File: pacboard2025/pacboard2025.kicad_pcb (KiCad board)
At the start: 4 copper layers, 80 x 80 mm, 28 parts, among them J1 XT30 Male Connector, U2 D24V50F5, U3 ProS3, U6 BNO085

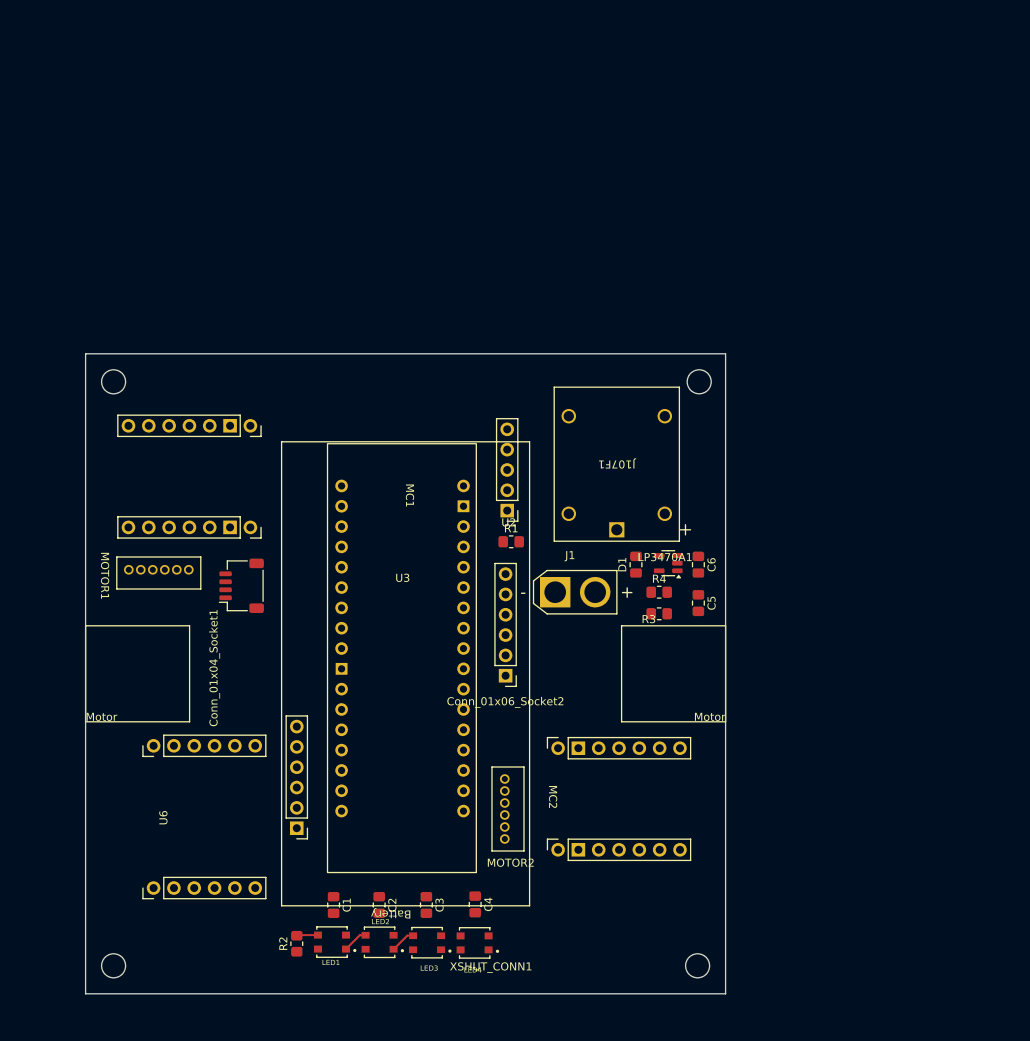
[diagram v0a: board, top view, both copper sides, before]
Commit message: changed layout
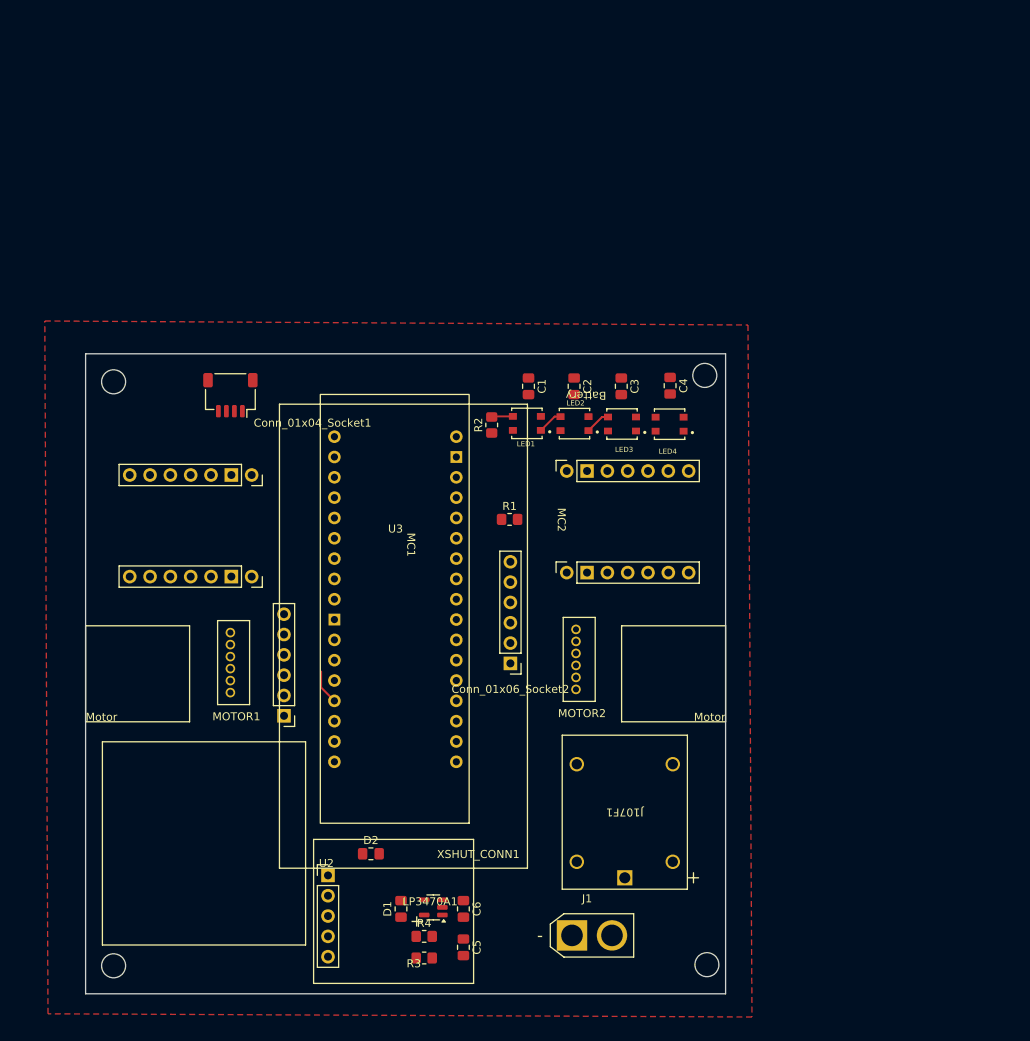
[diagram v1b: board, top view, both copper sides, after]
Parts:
- removed U6: BNO085, board1_footprints:BNU0085
- added D2: D, Capacitor_SMD:C_0805_2012Metric_Pad1.18x1.45mm_HandSolder, F.Cu at (115.7, 162.5)
- moved C1 69.3 mm to (135.4, 104.1)
- moved C2 69.3 mm to (141.1, 104.1)
- moved C3 69.3 mm to (147.0, 104.1)
- moved LED2 69.3 mm to (141.1, 108.7)
- moved LED3 69.3 mm to (147.1, 108.8)
- moved R2 69.3 mm to (130.8, 108.9)
- moved C4 69.3 mm to (153.1, 104.0)
- moved LED1 69.3 mm to (135.2, 108.7)
- moved LED4 69.3 mm to (153.0, 108.8)
- moved C5 52.1 mm to (127.2, 174.2)
- moved C6 52.1 mm to (127.2, 169.4)
- moved D1 52.1 mm to (119.4, 169.4)
- moved LP3470A1 52.1 mm to (123.5, 169.2)
- moved R3 52.1 mm to (122.3, 175.5)
- moved R4 52.1 mm to (122.3, 172.8)
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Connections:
- U2 pad 1: /5V -> Net-(D2-A)
- U3 pad 23: /UART_RX -> unconnected-(U3-RX-Pad23)
- U3 pad 24: /UART_TX -> unconnected-(U3-TX-Pad24)
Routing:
- net /XSHUT_TOF2: track 0.00 -> 4.34 mm
- added copper zone on In1.Cu, net /5V
- added copper zone on F.Cu, net /GND
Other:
- outline, holes or cut-outs redrawn

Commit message: Layout
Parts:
- moved MOTOR2 16.9 mm to (133.2, 149.3)
- moved XSHUT_CONN1 16.5 mm to (107.1, 128.9)
- moved MOTOR1 12.7 mm to (88.8, 126.1), turned to 90 degrees
- moved Conn_01x06_Socket2 10.4 mm to (133.4, 128.3)
- moved R1 9.20 mm to (133.1, 111.5)
- moved MC1 8.90 mm to (106.7, 112.6)
- moved Conn_01x04_Socket1 8.36 mm to (103.0, 98.4)
- moved U3 6.95 mm to (119.7, 123.8)
- moved C1 2.93 mm to (135.8, 101.2)
- moved C2 2.93 mm to (141.5, 101.2)
- moved C3 2.93 mm to (147.4, 101.2)
- moved LED1 2.93 mm to (135.6, 105.8)
- moved LED3 2.93 mm to (147.5, 105.9)
- moved R2 2.93 mm to (131.2, 106.0)
- moved C4 2.93 mm to (153.5, 101.1)
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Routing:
- net /XSHUT_TOF6: track 0.00 -> 99.7 mm
- net /2_ENCB: track 0.00 -> 46.2 mm
- net /5V: track 43.0 -> 0.11 mm
- net /1_ENCA: track 0.00 -> 41.7 mm, vias 0 -> 1
- net unconnected-(MC1-CS-Pad8): track 0.00 -> 35.9 mm, vias 0 -> 1
- net /1_ENCB: track 0.00 -> 35.1 mm, vias 0 -> 1
- net /SERIAL_CLOCK_LINE: track 0.00 -> 33.9 mm, vias 0 -> 1
- net /XSHUT_TOF3: track 0.00 -> 25.3 mm, vias 0 -> 1
- net /GND: track 0.00 -> 25.0 mm
- net /1_PWM2: track 0.00 -> 21.6 mm, vias 0 -> 1
- net /MOTOR2_V+: track 0.00 -> 19.7 mm
- net /XSHUT_TOF5: track 0.00 -> 12.9 mm
- net /XSHUT_TOF4: track 0.00 -> 12.9 mm
- net unconnected-(U3-IO0-Pad11): track 0.00 -> 9.03 mm
- net /INTR_TOF6: track 0.00 -> 9.03 mm
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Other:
- board size 80 x 80 mm -> 80 x 85 mm

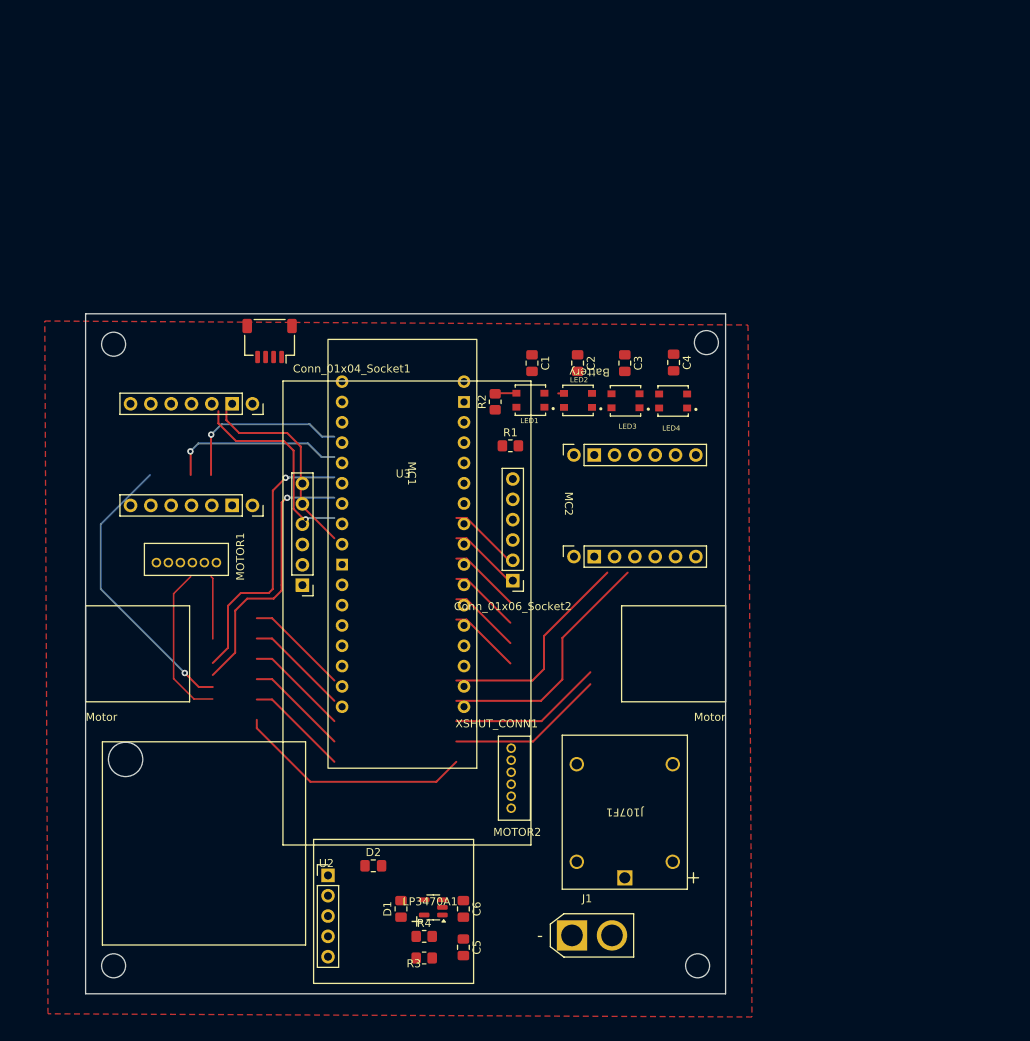
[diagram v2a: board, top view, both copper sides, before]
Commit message: layout updated
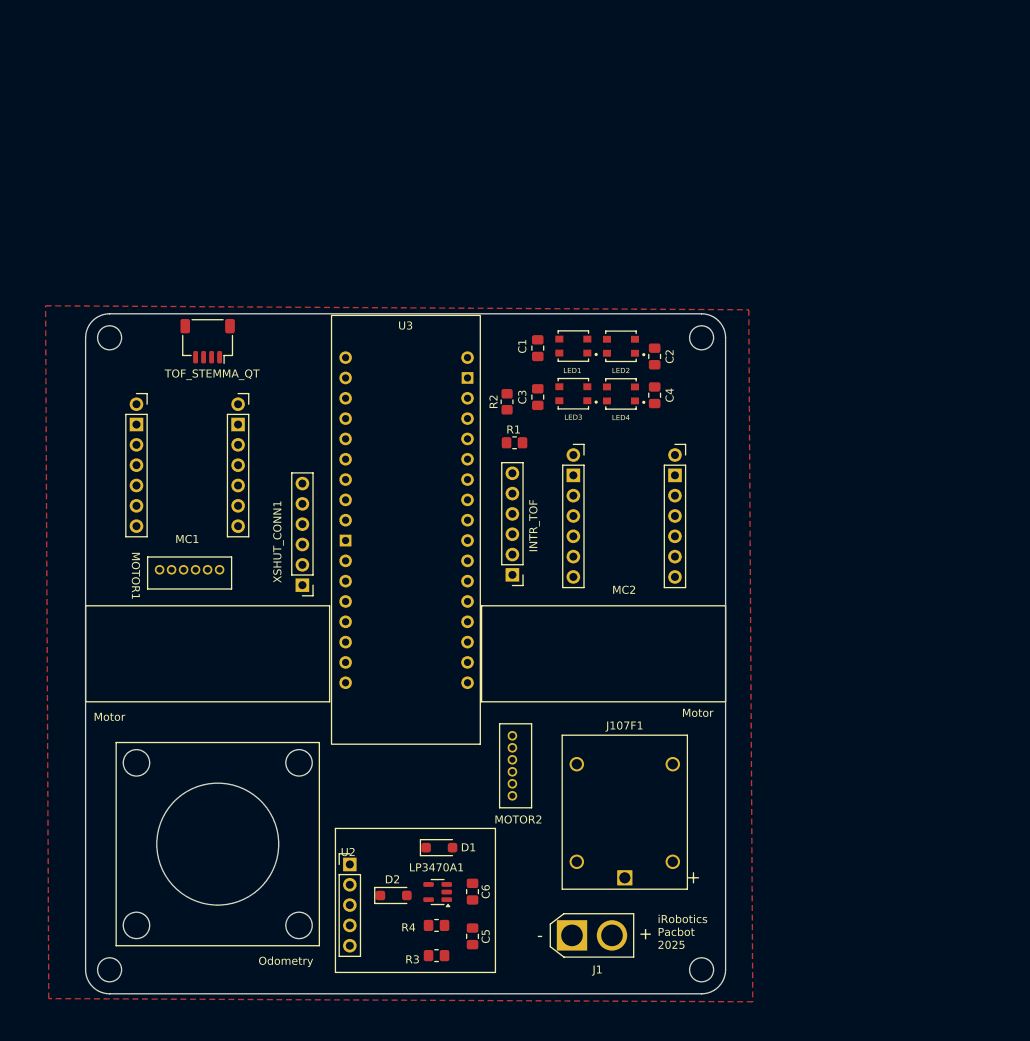
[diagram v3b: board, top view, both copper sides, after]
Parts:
- D1, D2: footprint Capacitor_SMD:C_0805_2012Metric_Pad1.18x1.45mm_HandSolder -> board1_footprints:SOD-123FL
- moved MC1 18.5 mm to (92.7, 100.4), turned to 0 degrees
- moved MC2 17.2 mm to (147.3, 106.8), turned to 0 degrees
- moved D1 13.7 mm to (124.4, 156.7), turned to 0 degrees
- moved C3 11.7 mm to (136.5, 105.4)
- moved C2 9.67 mm to (151.1, 100.3)
- moved LED1 8.64 mm to (141.0, 99.0)
- moved LED2 8.64 mm to (146.9, 99.1)
- moved MOTOR1 7.95 mm to (96.8, 127.0), turned to -90 degrees
- moved TOF_STEMMA_QT 7.75 mm to (95.2, 98.4)
- moved LED3 6.58 mm to (141.0, 105.0)
- moved LED4 6.58 mm to (146.9, 105.0)
- moved C4 4.73 mm to (151.1, 105.2)
- moved D2 3.05 mm to (118.7, 162.6)
- moved U2 3.05 mm to (113.0, 163.8)
- moved U3 3.03 mm to (120.1, 120.8)
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- renumbered Conn_01x06_Socket2 to INTR_TOF, Conn_01x04_Socket1 to TOF_STEMMA_QT
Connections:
- MOTOR1 pad 1: /MOTOR1_V+ -> /MOTOR1_V-
- MOTOR1 pad 2: /GND -> /+3.3V
- MOTOR1 pad 3: /1_ENCA -> /1_ENCB
- MOTOR1 pad 4: /1_ENCB -> /1_ENCA
- MOTOR1 pad 5: /+3.3V -> /GND
- MOTOR1 pad 6: /MOTOR1_V- -> /MOTOR1_V+
- MOTOR2 pad 1: /MOTOR2_V+ -> /MOTOR2_V-
- MOTOR2 pad 2: /GND -> /+3.3V
- MOTOR2 pad 3: /2_ENCA -> /2_ENCB
- MOTOR2 pad 4: /2_ENCB -> /2_ENCA
- MOTOR2 pad 5: /+3.3V -> /GND
- MOTOR2 pad 6: /MOTOR2_V- -> /MOTOR2_V+
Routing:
- net /XSHUT_TOF6: track 99.7 -> 0.00 mm
- net /2_ENCB: track 46.2 -> 0.00 mm
- net /1_ENCA: track 41.7 -> 0.00 mm, vias 1 -> 0
- net unconnected-(MC1-CS-Pad8): track 35.9 -> 0.00 mm, vias 1 -> 0
- net /1_ENCB: track 35.1 -> 0.00 mm, vias 1 -> 0
- net /SERIAL_CLOCK_LINE: track 33.9 -> 0.00 mm, vias 1 -> 0
- net /XSHUT_TOF3: track 25.3 -> 0.00 mm, vias 1 -> 0
- net /GND: track 25.0 -> 0.00 mm
- net /1_PWM2: track 21.6 -> 0.00 mm, vias 1 -> 0
- net /MOTOR2_V+: track 19.7 -> 0.00 mm
- net /XSHUT_TOF5: track 12.9 -> 0.00 mm
- net /XSHUT_TOF4: track 12.9 -> 0.00 mm
- net unconnected-(U3-IO0-Pad11): track 9.03 -> 0.00 mm
- net /INTR_TOF6: track 9.03 -> 0.00 mm
- net /INTR_TOF1: track 9.03 -> 0.00 mm
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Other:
- outline, holes or cut-outs redrawn
- board text added: "Odometry"
- board text added: "iRobotics Pacbot 2025"
- board text removed: "Battery"

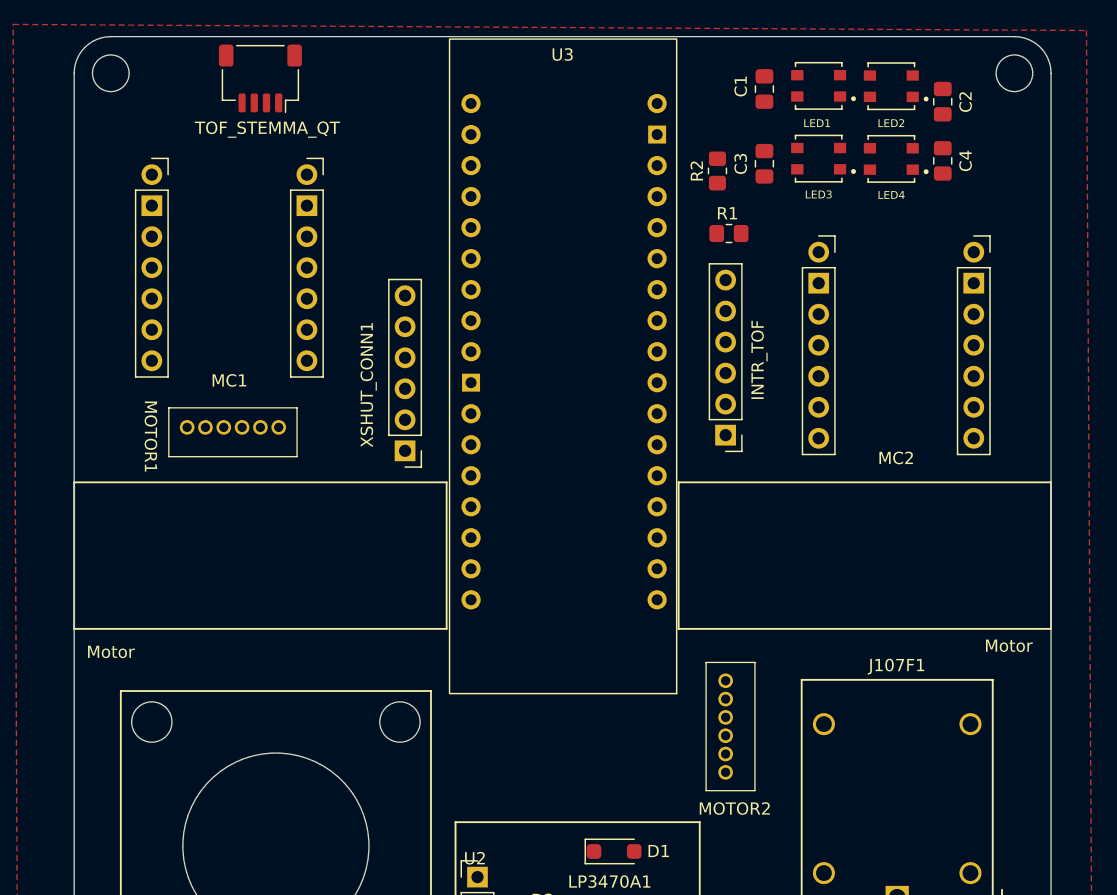
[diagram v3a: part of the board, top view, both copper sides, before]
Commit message: updated pcb layout, pros3 has pads
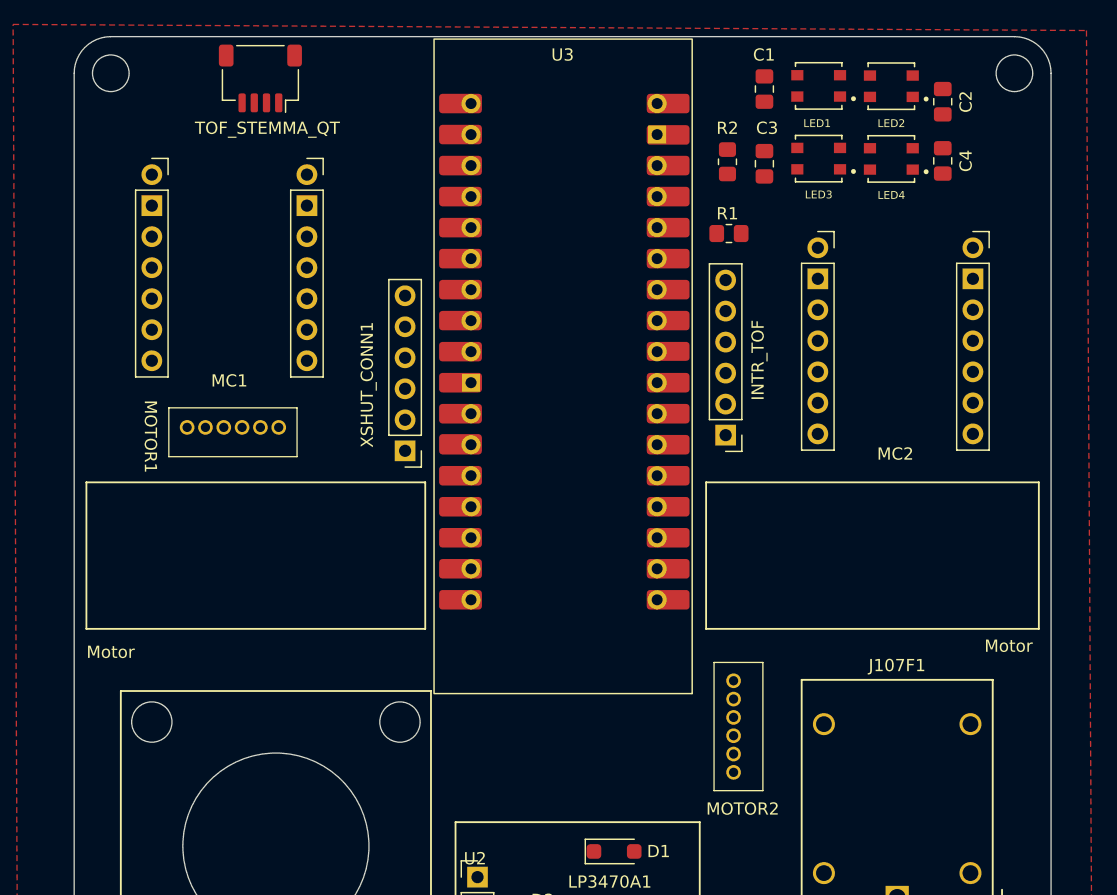
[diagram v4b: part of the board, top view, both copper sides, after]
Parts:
- moved R2 1.11 mm to (133.5, 105.2)
- moved MOTOR2 0.65 mm to (134.0, 147.8)
- moved MC2 0.37 mm to (147.2, 106.4)

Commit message: PCB with routing
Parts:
- moved R1 16.9 mm to (133.2, 128.1), turned to 90 degrees
- moved Conn_01x06_Socket2 4.18 mm to (133.1, 123.5)
- renumbered TOF_STEMMA_QT to Conn_01x04_Socket1, INTR_TOF to Conn_01x06_Socket2
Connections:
- MC1 pad 14: /+12V -> /12V
- MC2 pad 14: /+12V -> /12V
- U3 pad 4: /+3.3V -> unconnected-(U3-3V3-Pad4)
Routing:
- net /12V: track 0.00 -> 202.9 mm, vias 0 -> 2
- net /BAT_12V: track 0.00 -> 67.0 mm, vias 0 -> 3
- net /MOTOR2_V+: track 0.00 -> 46.0 mm
- net Net-(D1-A): track 0.00 -> 43.0 mm, vias 0 -> 2
- net /LED_DATA: track 0.00 -> 41.3 mm
- net /1_ENCA: track 0.00 -> 36.4 mm, vias 0 -> 2
- net /MOTOR2_V-: track 0.00 -> 36.0 mm
- net /XSHUT_TOF6: track 0.00 -> 35.8 mm, vias 0 -> 1
- net /1_ENCB: track 0.00 -> 35.6 mm
- net /1_PWM2: track 0.00 -> 29.8 mm
- net /1_PWM1: track 0.00 -> 29.8 mm
- net /GND: track 0.00 -> 29.7 mm, vias 0 -> 8
- net /XSHUT_TOF5: track 0.00 -> 29.4 mm, vias 0 -> 1
- net /SERIAL_CLOCK_LINE: track 0.00 -> 28.7 mm, vias 0 -> 2
- net /SERIAL_DATA_LINE: track 0.00 -> 27.4 mm, vias 0 -> 2
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- added copper zone on In2.Cu, net /+3.3V
- added copper zone on B.Cu, net /GND
